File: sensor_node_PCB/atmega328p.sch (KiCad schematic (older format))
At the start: 14 parts, among them SW1 RESET_SWITCH, U5 ATMEGA328P, X2 CSTCE16MOV53-R0

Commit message: added 3.3v regulator
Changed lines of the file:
@@
 $Descr A4 11693 8268
 encoding utf-8
-Sheet 2 4
+Sheet 2 3
 Title ""
 Date ""
@@
 AREF
 Wire Wire Line
-	4800 3750 5850 3750
+	4800 3750 5100 3750
 $Comp
 L Arduino_Uno_R3_From_Scratch-rescue:GND #PWR040
@@
 $EndComp
 Wire Wire Line
-	5600 4300 5600 4950
+	5600 4300 5600 4500
 Wire Wire Line
 	5600 4500 5850 4500
@@
 	5850 5500 5600 5500
 Wire Wire Line
-	5600 5250 5600 6050
+	5600 5250 5600 5500
 Wire Wire Line
 	5850 5700 5600 5700
@@
 SERIAL_Tx
 Wire Wire Line
-	8250 6100 9350 6100
+	8250 6100 8400 6100
 Wire Wire Line
 	8400 6100 8400 6275
@@
 	4600 5650 2850 5650
 Wire Wire Line
-	8250 5900 9350 5900
+	8250 5900 8550 5900
 Wire Wire Line
 	8550 5900 8550 6425
@@
 	9350 2100 8250 2100
 Wire Wire Line
-	8250 1900 9350 1900
-Wire Wire Line
-	8250 1700 9350 1700
-Wire Wire Line
-	8250 1500 9350 1500
+	8250 1900 8400 1900
+Wire Wire Line
+	8250 1700 8400 1700
+Wire Wire Line
+	8250 1500 8400 1500
 Text HLabel 1250 1500 0    40   Input ~ 0
 DTR
@@
 $EndComp
 Wire Wire Line
-	1250 1500 1900 1500
+	1250 1500 1550 1500
 Wire Wire Line
 	1550 1500 1550 1800
@@
 328P_RESET
 Wire Wire Line
-	2850 1500 5850 1500
+	2850 1500 3200 1500
 Wire Wire Line
 	4450 5900 4450 6425
@@
 $EndComp
 Wire Wire Line
-	4900 650  4900 1050
+	4900 650  4900 750
 Wire Wire Line
 	5300 1350 5300 1500
@@
 Connection ~ 4900 750
 Wire Wire Line
-	4050 750  5300 750
+	4050 750  4900 750
 Wire Wire Line
 	4350 950  4350 1100
@@
 $EndComp
 Wire Wire Line
-	5300 2050 5850 2050
+	5300 2050 5650 2050
 Wire Wire Line
 	5300 2050 5300 2150
@@
 	5300 2950 5300 3050
 Wire Wire Line
-	5300 3050 5850 3050
+	5300 3050 5650 3050
 Wire Wire Line
 	5050 2550 4750 2550
@@
 	3500 1650 3500 1775
 Wire Wire Line
-	3300 1650 3500 1650
+	3300 1650 3400 1650
 Wire Wire Line
 	3300 1775 3300 1650
@@
 	3500 2275 3500 2175
 Wire Wire Line
-	3300 2275 3500 2275
+	3300 2275 3400 2275
 Wire Wire Line
 	3300 2275 3300 2175
@@
 	1    0    0    -1
 $EndComp
+Wire Wire Line
+	5650 2050 5850 2050
+Wire Wire Line
+	5650 3050 5850 3050
+Wire Wire Line
+	5600 4500 5600 4700
+Wire Wire Line
+	5600 4700 5600 4950
+Wire Wire Line
+	5600 5700 5600 6050
+Wire Wire Line
+	5600 5500 5600 5700
+Wire Wire Line
+	5100 3750 5850 3750
+Wire Wire Line
+	8400 6100 9350 6100
+Wire Wire Line
+	8550 5900 9350 5900
+Wire Wire Line
+	1550 1500 1900 1500
+Wire Wire Line
+	5300 1500 5650 1500
+Wire Wire Line
+	4900 750  4900 1050
+Wire Wire Line
+	4900 750  5300 750
+Wire Wire Line
+	4900 1500 5300 1500
+Wire Wire Line
+	8400 1500 9350 1500
+Wire Wire Line
+	8400 1700 9350 1700
+Wire Wire Line
+	8400 1900 9350 1900
+Wire Wire Line
+	3200 1500 3400 1500
+Wire Wire Line
+	3400 1500 4900 1500
+Wire Wire Line
+	3400 1650 3500 1650
+Wire Wire Line
+	3400 2275 3500 2275
+Wire Wire Line
+	5650 1500 5850 1500
 $EndSCHEMATC

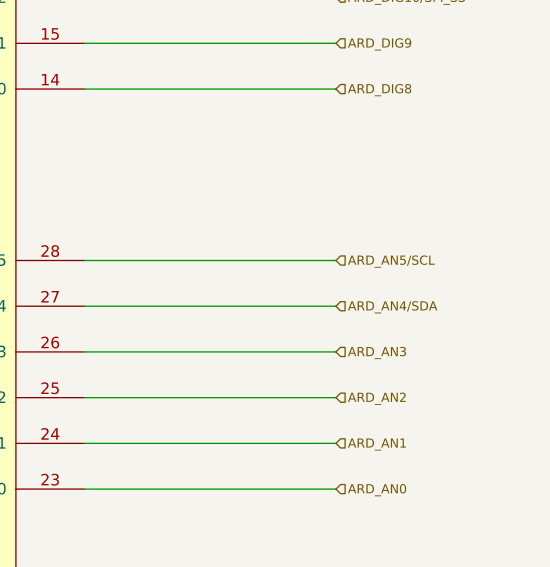
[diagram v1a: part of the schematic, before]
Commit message: changed bme280 to use i2c
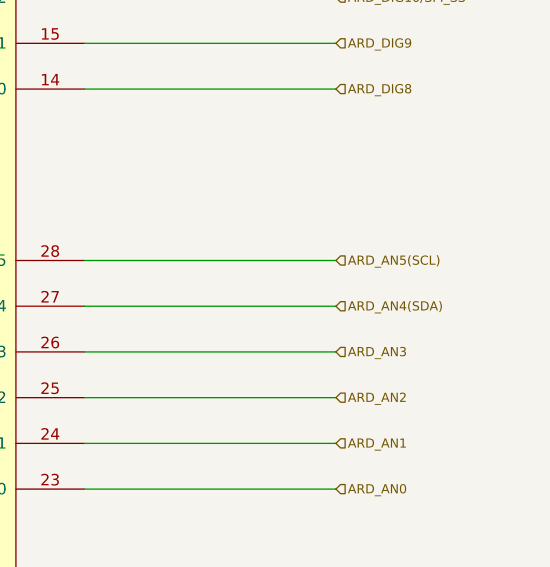
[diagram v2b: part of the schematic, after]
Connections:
- net ARD_AN4/SDA renamed ARD_AN4(SDA)
- net ARD_AN5/SCL renamed ARD_AN5(SCL)
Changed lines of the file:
@@
 	1250 5650 2550 5650
 Text HLabel 9350 3250 2    40   Input ~ 0
-ARD_AN5/SCL
+ARD_AN5(SCL)
 Text HLabel 9350 3450 2    40   Input ~ 0
-ARD_AN4/SDA
+ARD_AN4(SDA)
 Text HLabel 9350 3650 2    40   Input ~ 0
 ARD_AN3

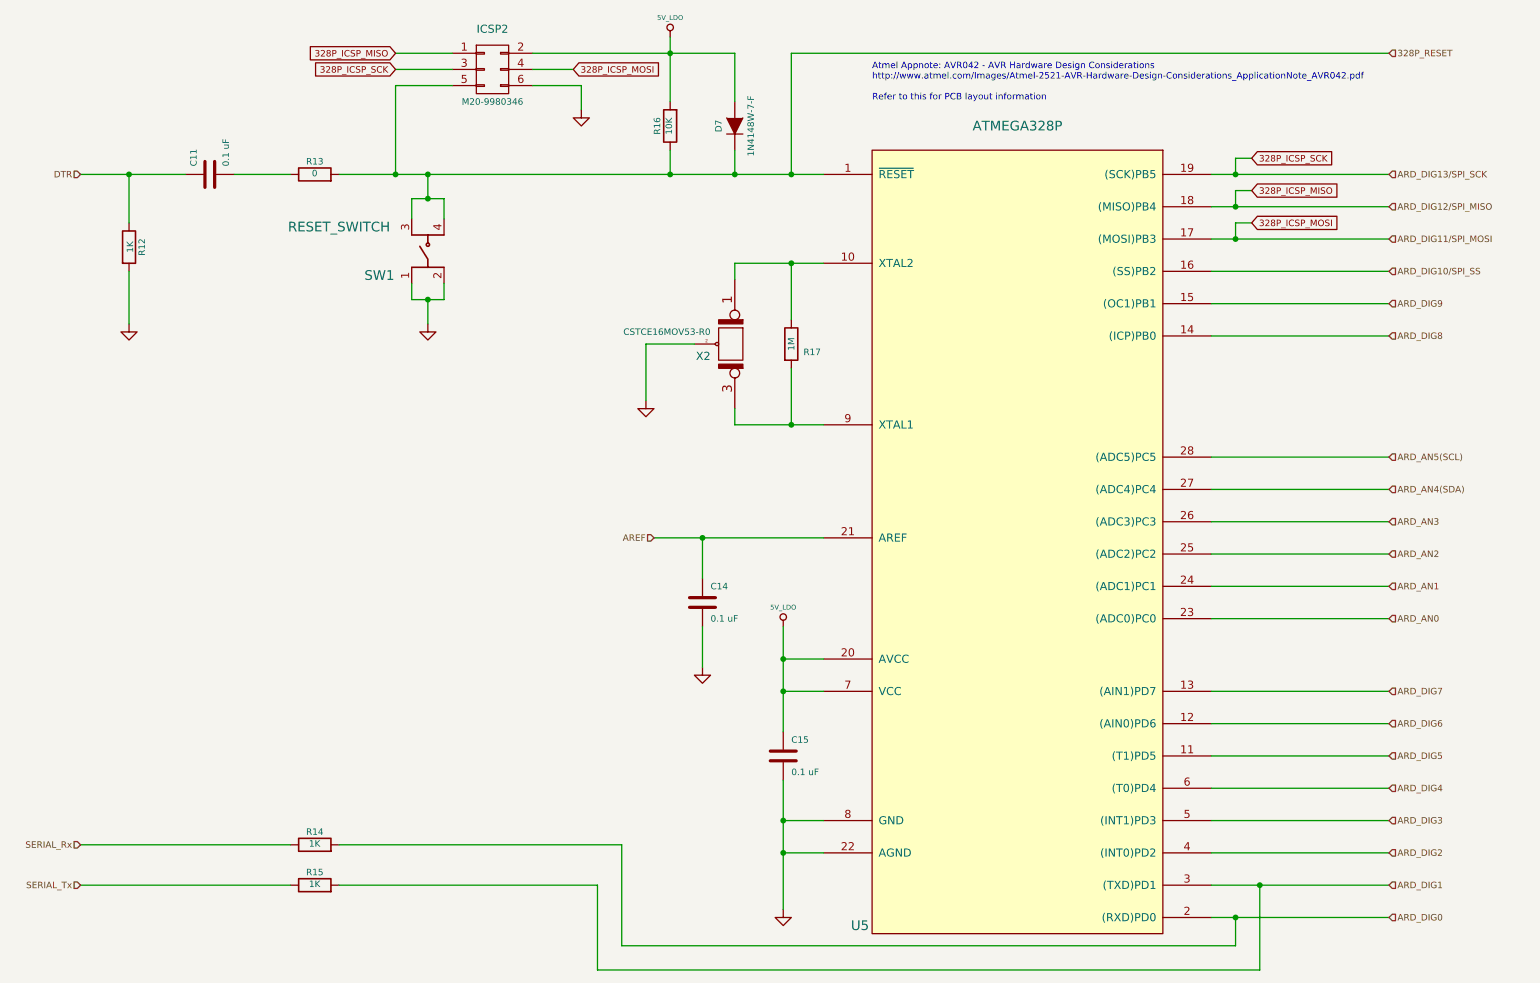
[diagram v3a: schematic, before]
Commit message: assign footprints 80% completed
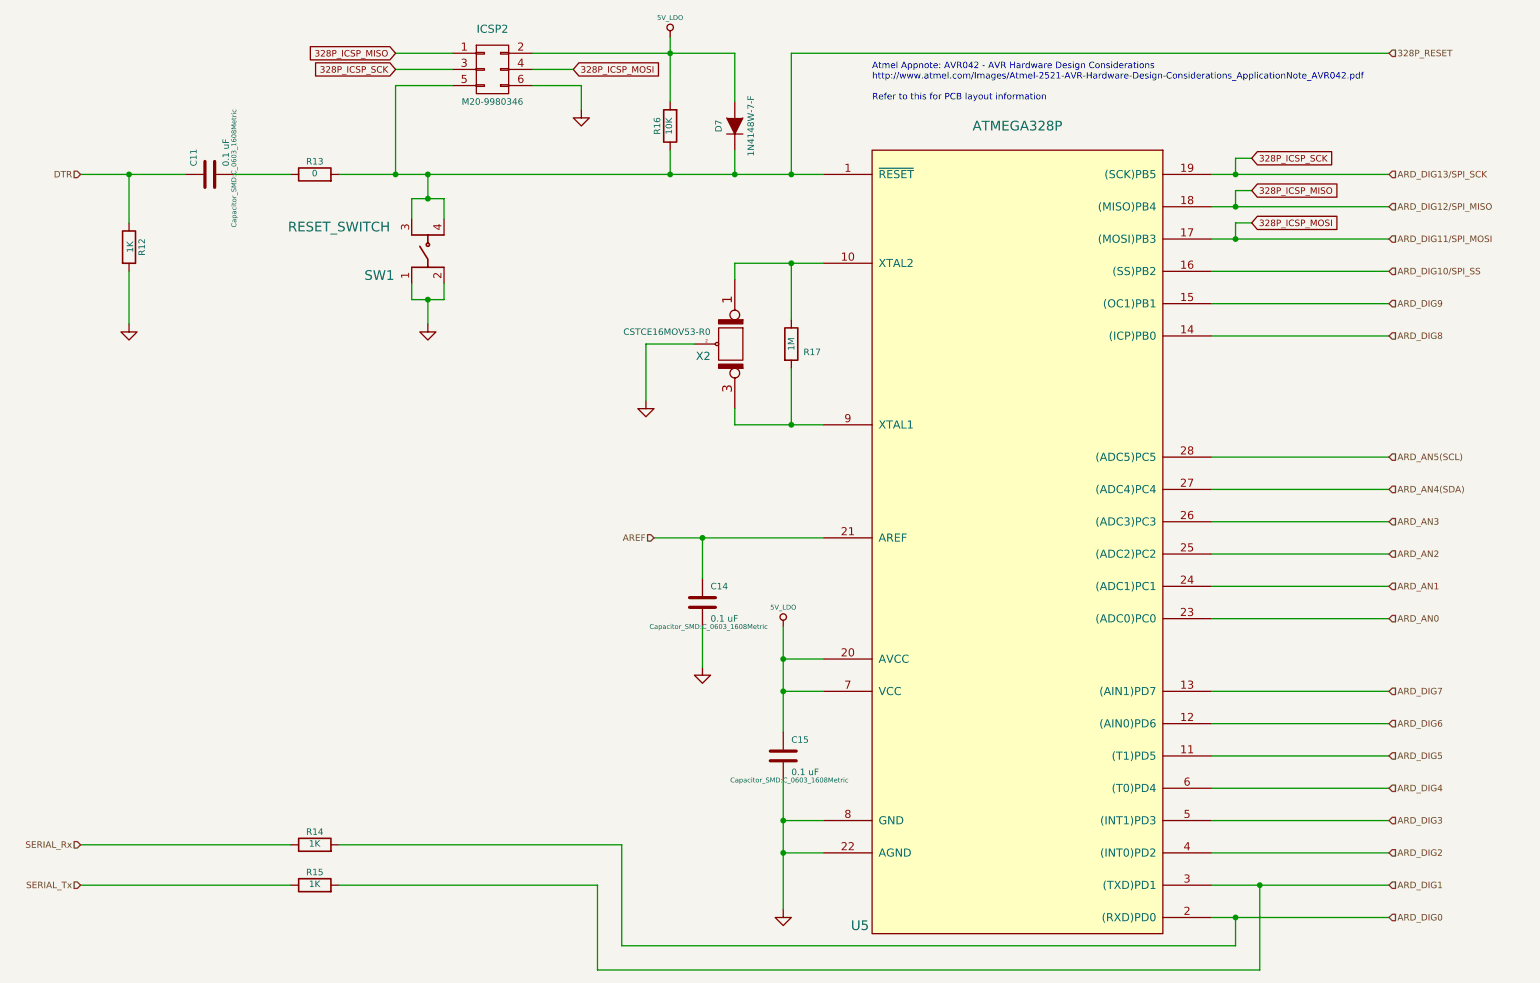
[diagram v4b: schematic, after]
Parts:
- C11, C14, C15: footprint ~ -> Capacitor_SMD:C_0603_1608Metric
- D7, ICSP2, X2: footprint ~ -> (none)
- R12, R13, R14, R15, R16, R17: footprint ~ -> Resistor_SMD:R_0603_1608Metric
- SW1: footprint (none) -> Button_Switch_THT:SW_TH_Tactile_Omron_B3F-10xx
- U5: footprint ~ -> Package_QFP:TQFP-32_7x7mm_P0.8mm
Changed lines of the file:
@@
 $Descr A4 11693 8268
 encoding utf-8
-Sheet 3 3
+Sheet 2 2
 Title ""
 Date ""
@@
 F 0 "U5" H 6075 1350 60  0000 C CNN
 F 1 "ATMEGA328P" H 7050 6300 60  0000 C CNN
-F 2 "~" H 6950 5250 60  0000 C CNN
+F 2 "Package_QFP:TQFP-32_7x7mm_P0.8mm" H 6950 5250 60  0001 C CNN
 F 3 "http://www.atmel.com/images/Atmel-8271-8-bit-AVR-Microcontroller-ATmega48A-48PA-88A-88PA-168A-168PA-328-328P_datasheet_Complete.pdf" H 6950 5250 60  0001 C CNN
 F 4 "IC MCU 8BIT 32KB FLASH 28DIP" H 7050 3750 60  0001 C CNN "Characteristics"
@@
 F 0 "R12" V 1630 1950 40  0000 C CNN
 F 1 "1K" V 1557 1951 40  0000 C CNN
-F 2 "~" V 1480 1950 30  0000 C CNN
+F 2 "Resistor_SMD:R_0603_1608Metric" V 1480 1950 30  0001 C CNN
 F 3 "http://images.ihscontent.net/vipimages/VipMasterIC/IC/VISH/VISHS75859/VISHS75859-1.pdf" H 1550 1950 30  0001 C CNN
 F 4 "METAL GLAZE/THICK FILM, 0.125W, 5%, 200ppm, 1000ohm, SURFACE MOUNT, 0805," H 1550 1950 60  0001 C CNN "Characteristics"
@@
 F 0 "ICSP2" H 3800 1100 50  0000 C CNN
 F 1 "M20-9980346" H 3800 650 40  0000 C CNN
-F 2 "~" H 3800 850 60  0000 C CNN
+F 2 "" H 3800 850 60  0001 C CNN
 F 3 "http://cdn.harwin.com/pdfs/M20-998.pdf" H 3800 850 60  0001 C CNN
 F 4 "6 CONTACT(S), MALE, STRAIGHT TWO PART BOARD CONNECTOR" H 3800 850 60  0001 C CNN "Characteristics"
@@
 F 0 "D7" H 5300 1300 40  0000 C CNN
 F 1 "1N4148W-7-F" H 5300 1100 40  0000 C CNN
-F 2 "~" H 5300 1200 60  0000 C CNN
+F 2 "" H 5300 1200 60  0001 C CNN
 F 3 "http://www.diodes.com/_files/datasheets/ds30086.pdf" H 5300 1200 60  0001 C CNN
 F 4 "DIODE GEN PURP 100V 300MA SOD123" H 5300 1200 60  0001 C CNN "Characteristics"
@@
 F 0 "SW1" V 3250 2275 60  0000 C CNN
 F 1 "RESET_SWITCH" V 3550 2525 60  0000 C CNN
-F 2 "" H 3400 1975 60  0000 C CNN
+F 2 "Button_Switch_THT:SW_TH_Tactile_Omron_B3F-10xx" H 3400 1975 60  0001 C CNN
 F 3 "http://industrial.panasonic.com/www-data/pdf/ATK0000/ATK0000CE28.pdf" H 3400 1975 60  0001 C CNN
 F 4 "SWITCH TACTILE SPST-NO 0.02A 15V" H 3400 1975 60  0001 C CNN "Characteristics"
@@
 F 0 "R13" V 2780 1500 40  0000 C CNN
 F 1 "0" V 2707 1501 40  0000 C CNN
-F 2 "~" V 2630 1500 30  0000 C CNN
+F 2 "Resistor_SMD:R_0603_1608Metric" V 2630 1500 30  0001 C CNN
 F 3 "http://industrial.panasonic.com/www-cgi/jvcr13pz.cgi?E+PZ+3+AOA0001+ERJ6GEY0R00V+7+WW" H 2700 1500 30  0001 C CNN
 F 4 "RES SMD 0.0 OHM JUMPER 1/8W 0805" H 2700 1500 60  0001 C CNN "Characteristics"
@@
 F 0 "X2" V 5325 2450 50  0000 R CNN
 F 1 "CSTCE16MOV53-R0" V 5175 2450 40  0000 R CNN
-F 2 "~" H 5250 2550 60  0000 C CNN
+F 2 "" H 5250 2550 60  0001 C CNN
 F 3 "http://www.murata.com/~/media/webrenewal/support/library/catalog/products/timingdevice/ceralock/p16e.ashx" H 5250 2550 60  0001 C CNN
 F 4 "CER RESONATOR 16.0MHZ SMD" H 5250 2550 60  0001 C CNN "Characteristics"
@@
 F 0 "C14" H 5150 4250 40  0000 L CNN
 F 1 "0.1 uF" H 5150 4050 40  0000 L CNN
-F 2 "~" H 5138 4000 30  0000 C CNN
+F 2 "Capacitor_SMD:C_0603_1608Metric" H 5138 4000 30  0000 C CNN
 F 3 "http://images.ihscontent.net/vipimages/VipMasterIC/IC/KEME/KEMES10043/KEMES10043-1.pdf" H 5100 4150 60  0001 C CNN
 F 4 "CAPACITOR, CERAMIC, MULTILAYER, 100 V, X7R, 0.1 uF, SURFACE MOUNT, 0805, CHIP, ROHS COMPLIANT" H 5100 4150 60  0001 C CNN "Characteristics"
@@
 F 0 "C15" H 5650 5200 40  0000 L CNN
 F 1 "0.1 uF" H 5650 5000 40  0000 L CNN
-F 2 "~" H 5638 4950 30  0000 C CNN
+F 2 "Capacitor_SMD:C_0603_1608Metric" H 5638 4950 30  0000 C CNN
 F 3 "http://images.ihscontent.net/vipimages/VipMasterIC/IC/KEME/KEMES10043/KEMES10043-1.pdf" H 5600 5100 60  0001 C CNN
 F 4 "CAPACITOR, CERAMIC, MULTILAYER, 100 V, X7R, 0.1 uF, SURFACE MOUNT, 0805, CHIP, ROHS COMPLIANT" H 5600 5100 60  0001 C CNN "Characteristics"
@@
 F 0 "R16" V 4980 1200 40  0000 C CNN
 F 1 "10K" V 4907 1201 40  0000 C CNN
-F 2 "~" V 4830 1200 30  0000 C CNN
+F 2 "Resistor_SMD:R_0603_1608Metric" V 4830 1200 30  0001 C CNN
 F 3 "http://images.ihscontent.net/vipimages/VipMasterIC/IC/VISH/VISHS75859/VISHS75859-1.pdf" H 4900 1200 30  0001 C CNN
 F 4 "RESISTOR, METAL GLAZE/THICK FILM, 0.125W, 5%, 200ppm, 10000ohm, SURFACE MOUNT, 0805" H 4900 1200 60  0001 C CNN "Characteristics"
@@
 F 0 "R14" V 2780 5650 40  0000 C CNN
 F 1 "1K" V 2707 5651 40  0000 C CNN
-F 2 "~" V 2630 5650 30  0000 C CNN
+F 2 "Resistor_SMD:R_0603_1608Metric" V 2630 5650 30  0001 C CNN
 F 3 "http://images.ihscontent.net/vipimages/VipMasterIC/IC/VISH/VISHS75859/VISHS75859-1.pdf" H 2700 5650 30  0001 C CNN
 F 4 "METAL GLAZE/THICK FILM, 0.125W, 5%, 200ppm, 1000ohm, SURFACE MOUNT, 0805," H 2700 5650 60  0001 C CNN "Characteristics"
@@
 F 0 "R15" V 2780 5900 40  0000 C CNN
 F 1 "1K" V 2707 5901 40  0000 C CNN
-F 2 "~" V 2630 5900 30  0000 C CNN
+F 2 "Resistor_SMD:R_0603_1608Metric" V 2630 5900 30  0001 C CNN
 F 3 "http://images.ihscontent.net/vipimages/VipMasterIC/IC/VISH/VISHS75859/VISHS75859-1.pdf" H 2700 5900 30  0001 C CNN
 F 4 "METAL GLAZE/THICK FILM, 0.125W, 5%, 200ppm, 1000ohm, SURFACE MOUNT, 0805," H 2700 5900 60  0001 C CNN "Characteristics"
@@
 F 0 "C11" H 2100 1600 40  0000 L CNN
 F 1 "0.1 uF" H 2100 1400 40  0000 L CNN
-F 2 "~" H 2088 1350 30  0000 C CNN
+F 2 "Capacitor_SMD:C_0603_1608Metric" H 2088 1350 30  0000 C CNN
 F 3 "http://images.ihscontent.net/vipimages/VipMasterIC/IC/KEME/KEMES10043/KEMES10043-1.pdf" H 2050 1500 60  0001 C CNN
 F 4 "CAPACITOR, CERAMIC, MULTILAYER, 100 V, X7R, 0.1 uF, SURFACE MOUNT, 0805, CHIP, ROHS COMPLIANT" H 2050 1500 60  0001 C CNN "Characteristics"
@@
 F 0 "R17" H 5725 2500 40  0000 L CNN
 F 1 "1M" V 5650 2550 40  0000 C CNN
-F 2 "~" V 5580 2550 30  0000 C CNN
+F 2 "Resistor_SMD:R_0603_1608Metric" V 5580 2550 30  0001 C CNN
 F 3 "http://www.vishay.com/docs/20035/dcrcwe3.pdf" H 5650 2550 30  0001 C CNN
 F 4 "RES SMD 1M OHM 1% 1/8W 0805" H 5650 2550 60  0001 C CNN "Characteristics"
